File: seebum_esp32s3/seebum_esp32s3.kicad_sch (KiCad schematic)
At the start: 12 parts, among them J101 Conn_01x02_Pin, J102 Conn_01x04_Pin, J103 Conn_01x02_Pin, Q101 AO4407, SW101 SW_DPDT_x2

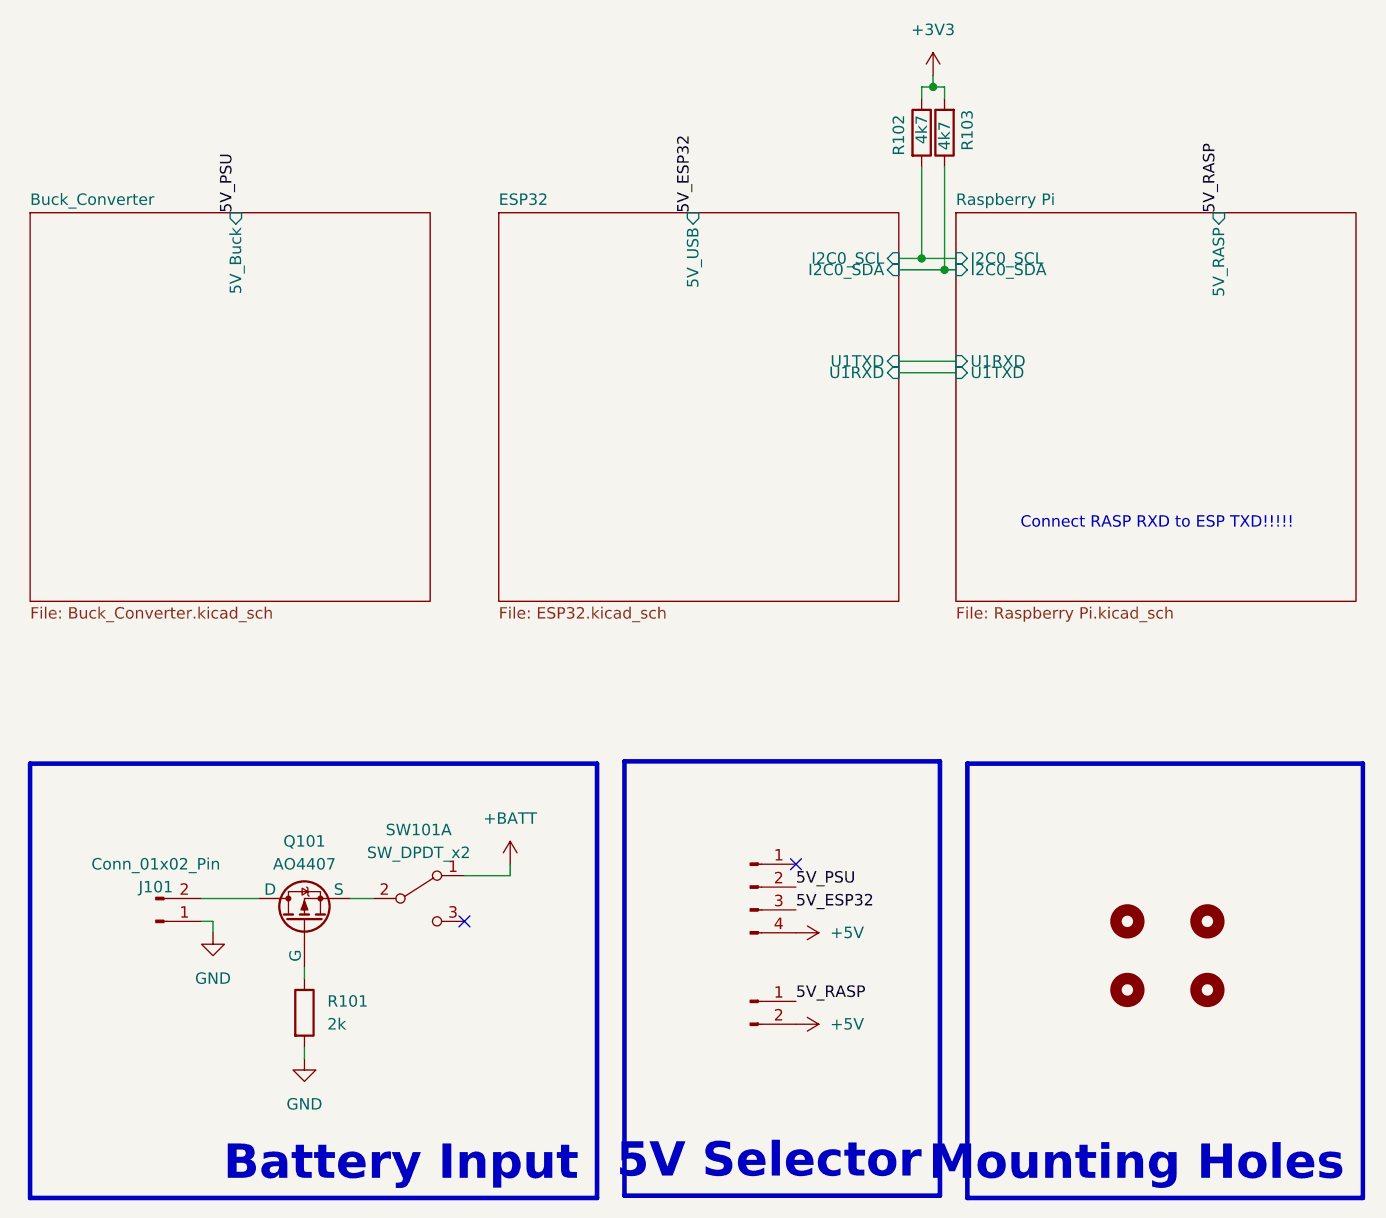
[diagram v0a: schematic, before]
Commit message: Feat: fix uart1 schematic issue and I2C redundancy
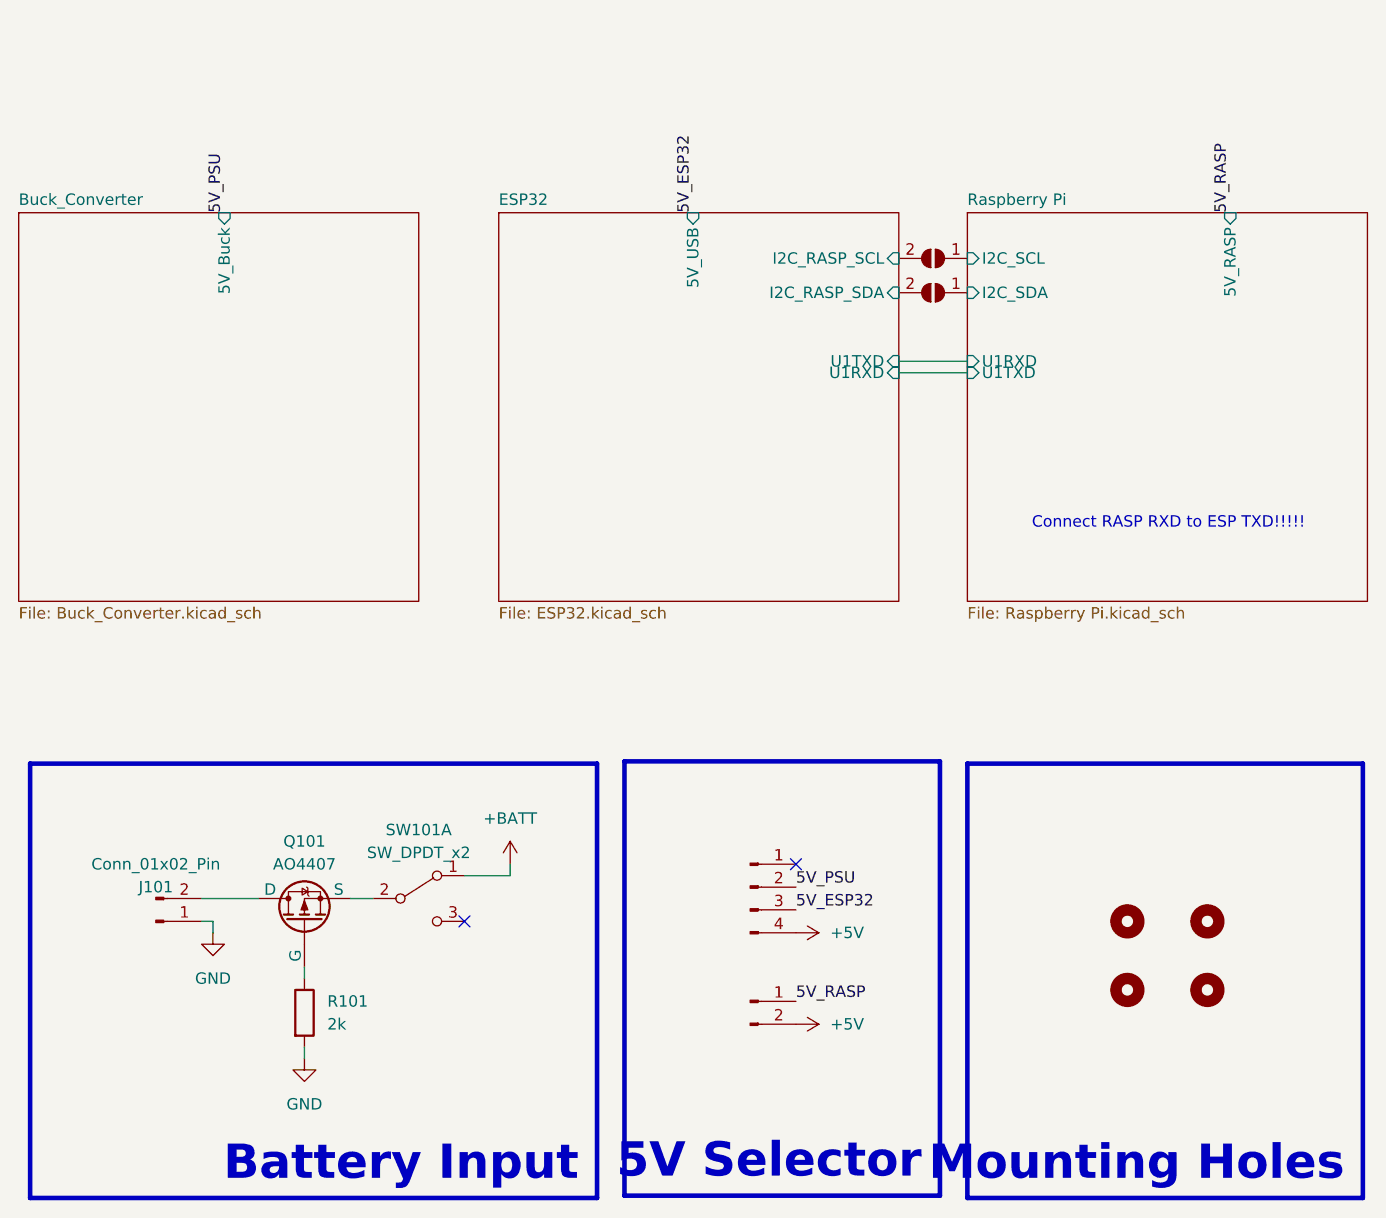
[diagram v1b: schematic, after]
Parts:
- removed R102, R103: 4k7, Resistor_SMD:R_0805_2012Metric, symbol Device:R
- added JP101, JP102: SolderJumper_2_Open, Jumper:SolderJumper-2_P1.3mm_Open_TrianglePad1.0x1.5mm, symbol Jumper:SolderJumper_2_Open
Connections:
- new net ESP32/I2C_RASP_SCL: JP101.2 (B)
- new net ESP32/I2C_RASP_SDA: JP102.2 (B)
- new net Raspberry Pi/I2C_SCL: JP101.1 (A)
- new net Raspberry Pi/I2C_SDA: JP102.1 (A)
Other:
- sheet ESP32 ports: added I2C_RASP_SCL, I2C_RASP_SDA; removed I2C0_SCL, I2C0_SDA
- sheet Raspberry Pi ports: added I2C_SCL, I2C_SDA; removed I2C0_SCL, I2C0_SDA

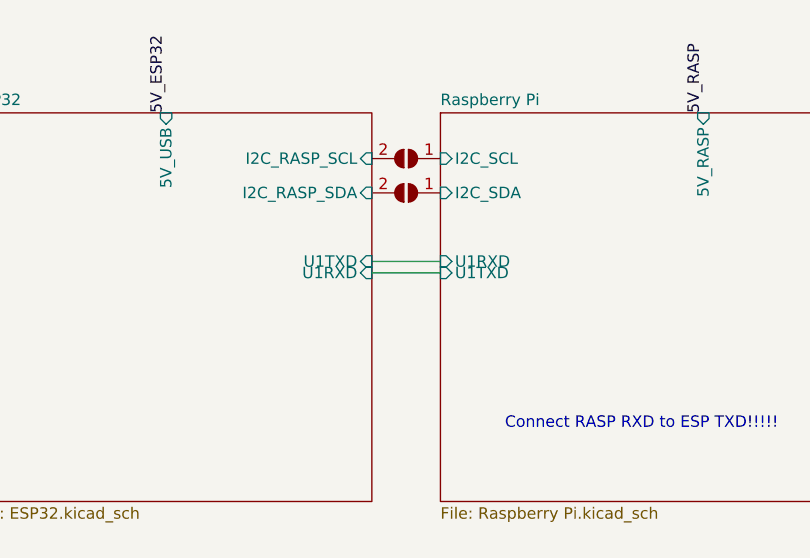
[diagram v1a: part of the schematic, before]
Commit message: Feat: I2C and UART to same pins in ESP32, since any GPIO can be RxD and TxD
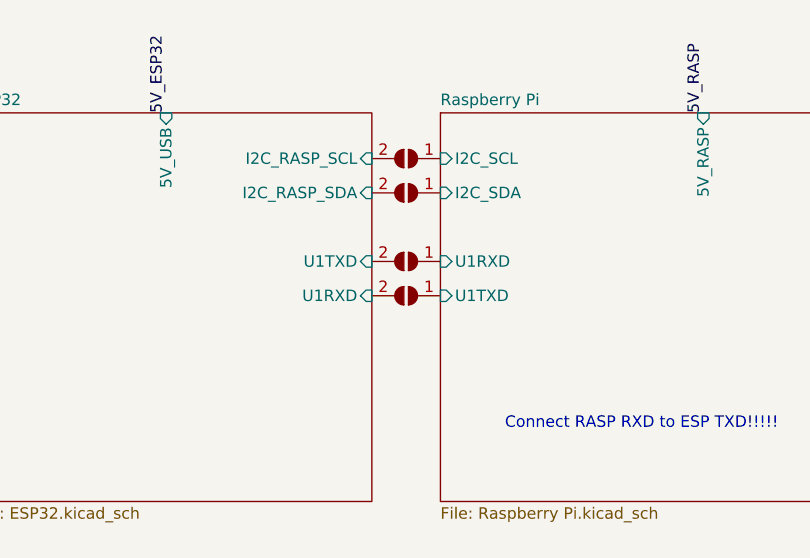
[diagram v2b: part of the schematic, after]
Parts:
- added JP103, JP104: SolderJumper_2_Open, Jumper:SolderJumper-2_P1.3mm_Bridged_RoundedPad1.0x1.5mm, symbol Jumper:SolderJumper_2_Open
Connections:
- net ESP32/U1RXD: now also JP104.2 (B)
- net ESP32/U1TXD: now also JP103.2 (B)
- new net Raspberry Pi/U1RXD: JP103.1 (A)
- new net Raspberry Pi/U1TXD: JP104.1 (A)
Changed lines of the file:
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@@
 	(wire
 		(pts
-			(xy 171.45 58.42) (xy 179.07 58.42)
+			(xy 105.41 124.46) (xy 105.41 125.73)
 		)
 		(stroke
@@
 	(wire
 		(pts
-			(xy 105.41 124.46) (xy 105.41 125.73)
+			(xy 110.49 116.84) (xy 113.03 116.84)
 		)
 		(stroke
@@
 	(wire
 		(pts
-			(xy 110.49 116.84) (xy 113.03 116.84)
-		)
-		(stroke
-			(width 0)
-			(type default)
-		)
-	)
-	(wire
-		(pts
 			(xy 95.25 119.38) (xy 95.25 120.65)
-		)
-		(stroke
-			(width 0)
-			(type default)
-		)
-	)
-	(wire
-		(pts
-			(xy 171.45 57.15) (xy 179.07 57.15)
 		)
 		(stroke
@@
 	)
 	(symbol
+		(lib_id "Jumper:SolderJumper_2_Open")
+		(at 175.26 60.96 180)
+		(unit 1)
+		(exclude_from_sim no)
+		(in_bom yes)
+		(on_board yes)
+		(dnp no)
+		(property "Reference" "JP104"
+			(at 176.5301 63.5 90)
+			(effects
+				(font
+					(size 1.27 1.27)
+				)
+				(justify left)
+				(hide yes)
+			)
+		)
+		(property "Value" "SolderJumper_2_Open"
+			(at 181.61 58.42 0)
+			(effects
+				(font
+					(size 1.27 1.27)
+				)
+				(justify left)
+				(hide yes)
+			)
+		)
+		(property "Footprint" "Jumper:SolderJumper-2_P1.3mm_Bridged_RoundedPad1.0x1.5mm"
+			(at 175.26 60.96 0)
+			(effects
+				(font
+					(size 1.27 1.27)
+				)
+				(hide yes)
+			)
+		)
+		(property "Datasheet" "~"
+			(at 175.26 60.96 0)
+			(effects
+				(font
+					(size 1.27 1.27)
+				)
+				(hide yes)
+			)
+		)
+		(property "Description" ""
+			(at 175.26 60.96 0)
+			(effects
+				(font
+					(size 1.27 1.27)
+				)
+				(hide yes)
+			)
+		)
+		(pin "1"
+		)
+		(pin "2"
+		)
+		(instances
+			(project "seebum_esp32s3"
+				(path "/4eaa6483-1d2f-48d6-89f0-93b42e27355e"
+					(reference "JP104")
+					(unit 1)
+				)
+			)
+		)
+	)
+	(symbol
 		(lib_id "power:+5V")
 		(at 160.02 120.65 270)
@@
 				(path "/4eaa6483-1d2f-48d6-89f0-93b42e27355e"
 					(reference "H104")
+					(unit 1)
+				)
+			)
+		)
+	)
+	(symbol
+		(lib_id "Jumper:SolderJumper_2_Open")
+		(at 175.26 57.15 180)
+		(unit 1)
+		(exclude_from_sim no)
+		(in_bom yes)
+		(on_board yes)
+		(dnp no)
+		(property "Reference" "JP103"
+			(at 176.5301 59.69 90)
+			(effects
+				(font
+					(size 1.27 1.27)
+				)
+				(justify left)
+				(hide yes)
+			)
+		)
+		(property "Value" "SolderJumper_2_Open"
+			(at 181.61 54.61 0)
+			(effects
+				(font
+					(size 1.27 1.27)
+				)
+				(justify left)
+				(hide yes)
+			)
+		)
+		(property "Footprint" "Jumper:SolderJumper-2_P1.3mm_Bridged_RoundedPad1.0x1.5mm"
+			(at 175.26 57.15 0)
+			(effects
+				(font
+					(size 1.27 1.27)
+				)
+				(hide yes)
+			)
+		)
+		(property "Datasheet" "~"
+			(at 175.26 57.15 0)
+			(effects
+				(font
+					(size 1.27 1.27)
+				)
+				(hide yes)
+			)
+		)
+		(property "Description" ""
+			(at 175.26 57.15 0)
+			(effects
+				(font
+					(size 1.27 1.27)
+				)
+				(hide yes)
+			)
+		)
+		(pin "1"
+		)
+		(pin "2"
+		)
+		(instances
+			(project "seebum_esp32s3"
+				(path "/4eaa6483-1d2f-48d6-89f0-93b42e27355e"
+					(reference "JP103")
 					(unit 1)
 				)
@@
 		)
 		(pin "U1RXD" input
-			(at 171.45 58.42 0)
+			(at 171.45 60.96 0)
 			(effects
 				(font
@@
 		)
 		(pin "U1TXD" input
-			(at 179.07 58.42 180)
-			(effects
-				(font
+			(at 179.07 60.96 180)
+			(effects
+				(font
